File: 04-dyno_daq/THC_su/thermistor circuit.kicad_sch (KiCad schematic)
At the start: 10 parts, among them J1 Conn_01x04, J2 Conn_01x02, U1 INA333xxDGK

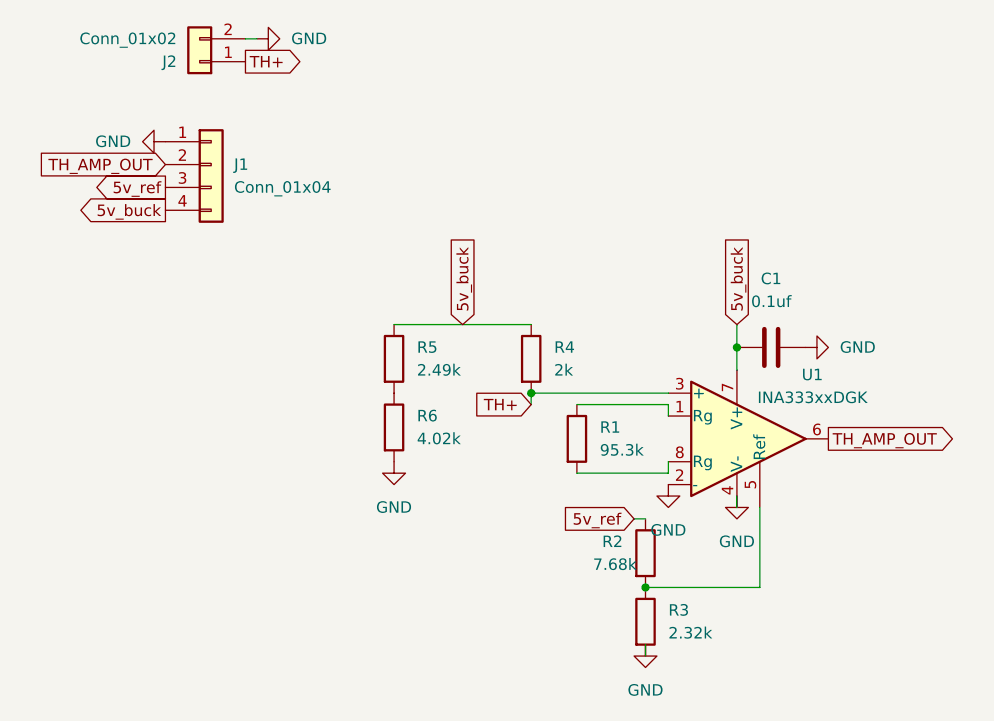
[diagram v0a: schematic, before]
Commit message: Updated grounding for temp pcbs
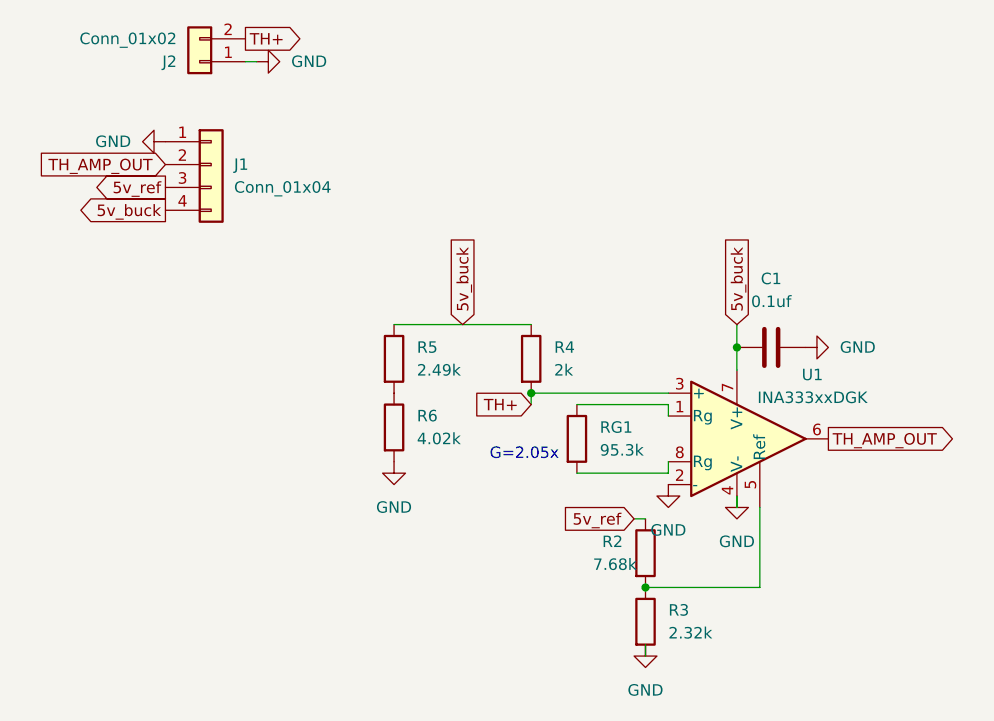
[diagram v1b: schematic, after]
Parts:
- renumbered R1 to RG1
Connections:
- net GND: now also J2.1 (Pin_1); no longer J2.2 (Pin_2)
- net TH+: now also J2.2 (Pin_2); no longer J2.1 (Pin_1)
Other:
- note added: "G=2.05x"
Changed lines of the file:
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@@
 	(generator_version "9.0")
 	(paper "A4")
+	(text "G=2.05x"
+		(exclude_from_sim no)
+		(at 123.698 95.758 0)
+		(effects
+			(font
+				(size 1.27 1.27)
+			)
+		)
+	)
 	(junction
 		(at 137.16 110.49)
@@
 	(wire
 		(pts
+			(xy 93.98 52.07) (xy 92.71 52.07)
+		)
+		(stroke
+			(width 0)
+			(type default)
+		)
+	)
+	(wire
+		(pts
 			(xy 149.86 101.6) (xy 149.86 110.49)
 		)
@@
 		(pts
 			(xy 135.89 102.87) (xy 137.16 102.87)
-		)
-		(stroke
-			(width 0)
-			(type default)
-		)
-	)
-	(wire
-		(pts
-			(xy 93.98 49.53) (xy 92.71 49.53)
 		)
 		(stroke
@@
 		)
 	)
-	(global_label "TH+"
-		(shape output)
-		(at 92.71 52.07 0)
-		(fields_autoplaced yes)
-		(effects
-			(font
-				(size 1.27 1.27)
-			)
-			(justify left)
-		)
-		(property "Intersheetrefs" "${INTERSHEET_REFS}"
-			(at 99.5657 52.07 0)
-			(effects
-				(font
-					(size 1.27 1.27)
-				)
-				(justify left)
-				(hide yes)
-			)
-		)
-	)
 	(global_label "5v_ref"
 		(shape output)
@@
 		(property "Intersheetrefs" "${INTERSHEET_REFS}"
 			(at 172.1371 93.98 0)
+			(effects
+				(font
+					(size 1.27 1.27)
+				)
+				(justify left)
+				(hide yes)
+			)
+		)
+	)
+	(global_label "TH+"
+		(shape output)
+		(at 92.71 49.53 0)
+		(fields_autoplaced yes)
+		(effects
+			(font
+				(size 1.27 1.27)
+			)
+			(justify left)
+		)
+		(property "Intersheetrefs" "${INTERSHEET_REFS}"
+			(at 99.5657 49.53 0)
 			(effects
 				(font
@@
 		(dnp no)
 		(fields_autoplaced yes)
-		(property "Reference" "R1"
+		(property "Reference" "RG1"
 			(at 132.08 92.7099 0)
 			(effects
@@
 			(project "thermistor circuit"
 				(path "/9ed712a9-952b-4eb0-a3d6-b0aaca0ca0fd"
-					(reference "R1")
+					(reference "RG1")
 					(unit 1)
 				)
@@
 	(symbol
 		(lib_id "power:GND")
-		(at 93.98 49.53 90)
+		(at 93.98 52.07 90)
 		(unit 1)
 		(exclude_from_sim no)
@@
 		(fields_autoplaced yes)
 		(property "Reference" "#PWR01"
-			(at 100.33 49.53 0)
+			(at 100.33 52.07 0)
 			(effects
 				(font
@@
 		)
 		(property "Value" "GND"
-			(at 97.79 49.5299 90)
+			(at 97.79 52.0699 90)
 			(effects
 				(font
@@
 		)
 		(property "Footprint" ""
-			(at 93.98 49.53 0)
+			(at 93.98 52.07 0)
 			(effects
 				(font
@@
 		)
 		(property "Datasheet" ""
-			(at 93.98 49.53 0)
+			(at 93.98 52.07 0)
 			(effects
 				(font
@@
 		)
 		(property "Description" "Power symbol creates a global label with name \"GND\" , ground"
-			(at 93.98 49.53 0)
+			(at 93.98 52.07 0)
 			(effects
 				(font
@@
 		)
 		(instances
-			(project ""
+			(project "thermistor circuit"
 				(path "/9ed712a9-952b-4eb0-a3d6-b0aaca0ca0fd"
 					(reference "#PWR01")
